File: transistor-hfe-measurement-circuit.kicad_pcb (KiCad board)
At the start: 4 copper layers, 100 x 60 mm, 97 parts, among them J1 Barrel_Jack_Switch, J2 B-057-HP, J3 B-057-HP, J4 2227MC-06-03, J5 B-057-HP, J6 B-057-HP, Q1 HL2303, Q2 SS8550 Y2, Q3 HL2303, Q4 SSM6L56FE, SW1 SW_DPDT_x2, SW2 SW_DPDT_x2, U1 NJM11100F1, U2 74HC14D,653, U3 OPA2333AIDR, U4 REF35102QDBVR

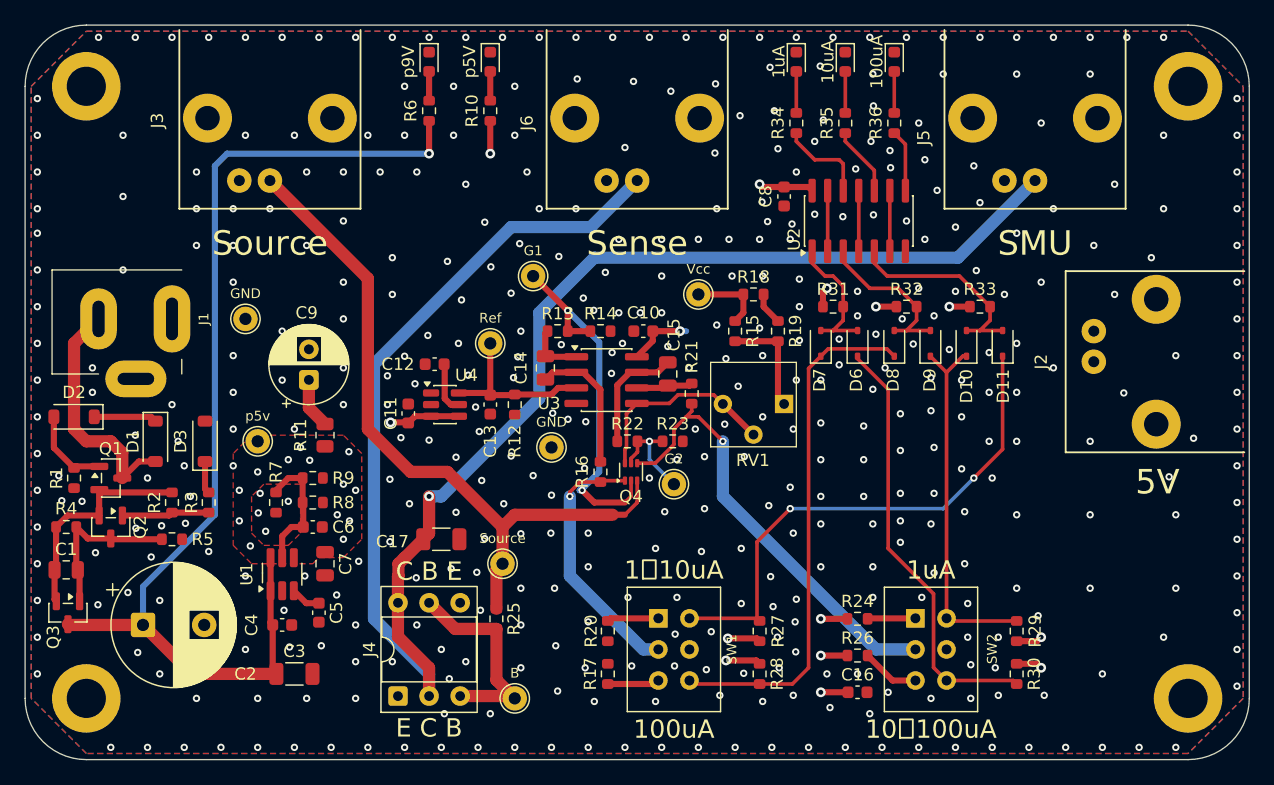
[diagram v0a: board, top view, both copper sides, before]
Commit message: feat: v1.1 として現行版の定電流回路を取り込む
HVRF リポジトリの作業ツリー（2026-10-15 時点）を v1.1 として取り込む。

- プロジェクトを transistor-hfe-measurement-circuit に改名
  （サブシートは cc-component.kicad_sch）
- 回路図・PCB のタイトルブロックに版数・著作権・ライセンス
  （CERN-OHL-P v2）・リポジトリ URL を入れる
- 基板シルクの版数を V1.0 から V1.1 にする
- PCB にはメーカー製 3D モデルを埋め込まず、DC ジャックは自作の
  簡易モデルを参照する

Co-Authored-By: Claude Opus 5.5 <noreply@anthropic.com>
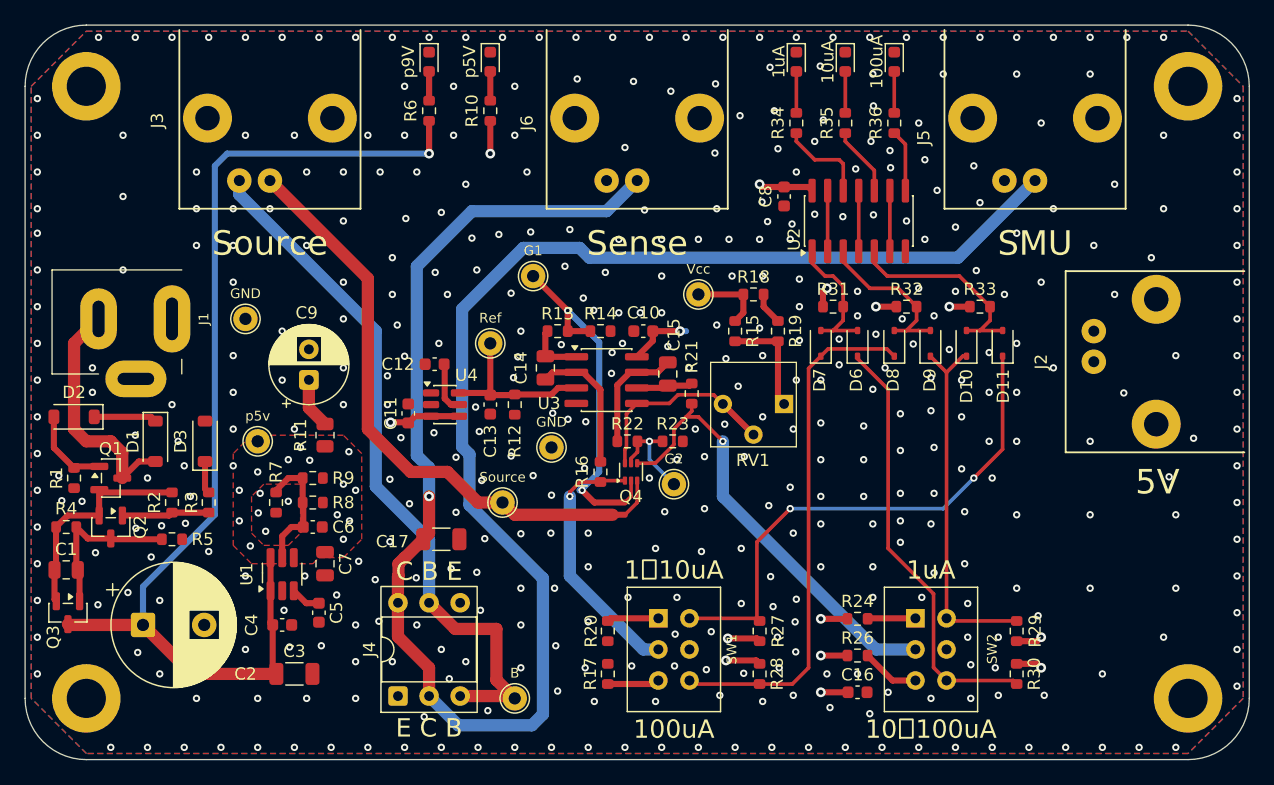
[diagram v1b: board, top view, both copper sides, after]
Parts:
- removed R25: 0, Resistor_SMD:R_0603_1608Metric
- moved TP6 5.00 mm to (68.6, 80.5)
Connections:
- J3 pad 2: GNDPWR -> Net-(J3-Ext)
- J4 pad 3: Net-(J4-Pin_3) -> Net-(J3-Ext)
- J4 pad 5: Net-(J4-Pin_3) -> Net-(J3-Ext)
- TP9 pad 1: Net-(J4-Pin_3) -> Net-(J3-Ext)
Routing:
- net Net-(J3-Ext): track 0.00 -> 58.1 mm
- net Net-(J4-Pin_2): track 139.4 -> 156.9 mm
- net Net-(J4-Pin_3): track 17.2 -> 0.00 mm
- net Net-(J3-In): track 58.4 -> 50.7 mm
- net GNDPWR: vias 432 -> 434
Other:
- board text added: "Transistor hFE measurement circuit V1.1"
- board text removed: "Transistor hFE measurement circuit V1.0"
